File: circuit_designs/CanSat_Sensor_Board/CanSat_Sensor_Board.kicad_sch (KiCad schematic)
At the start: 19 parts

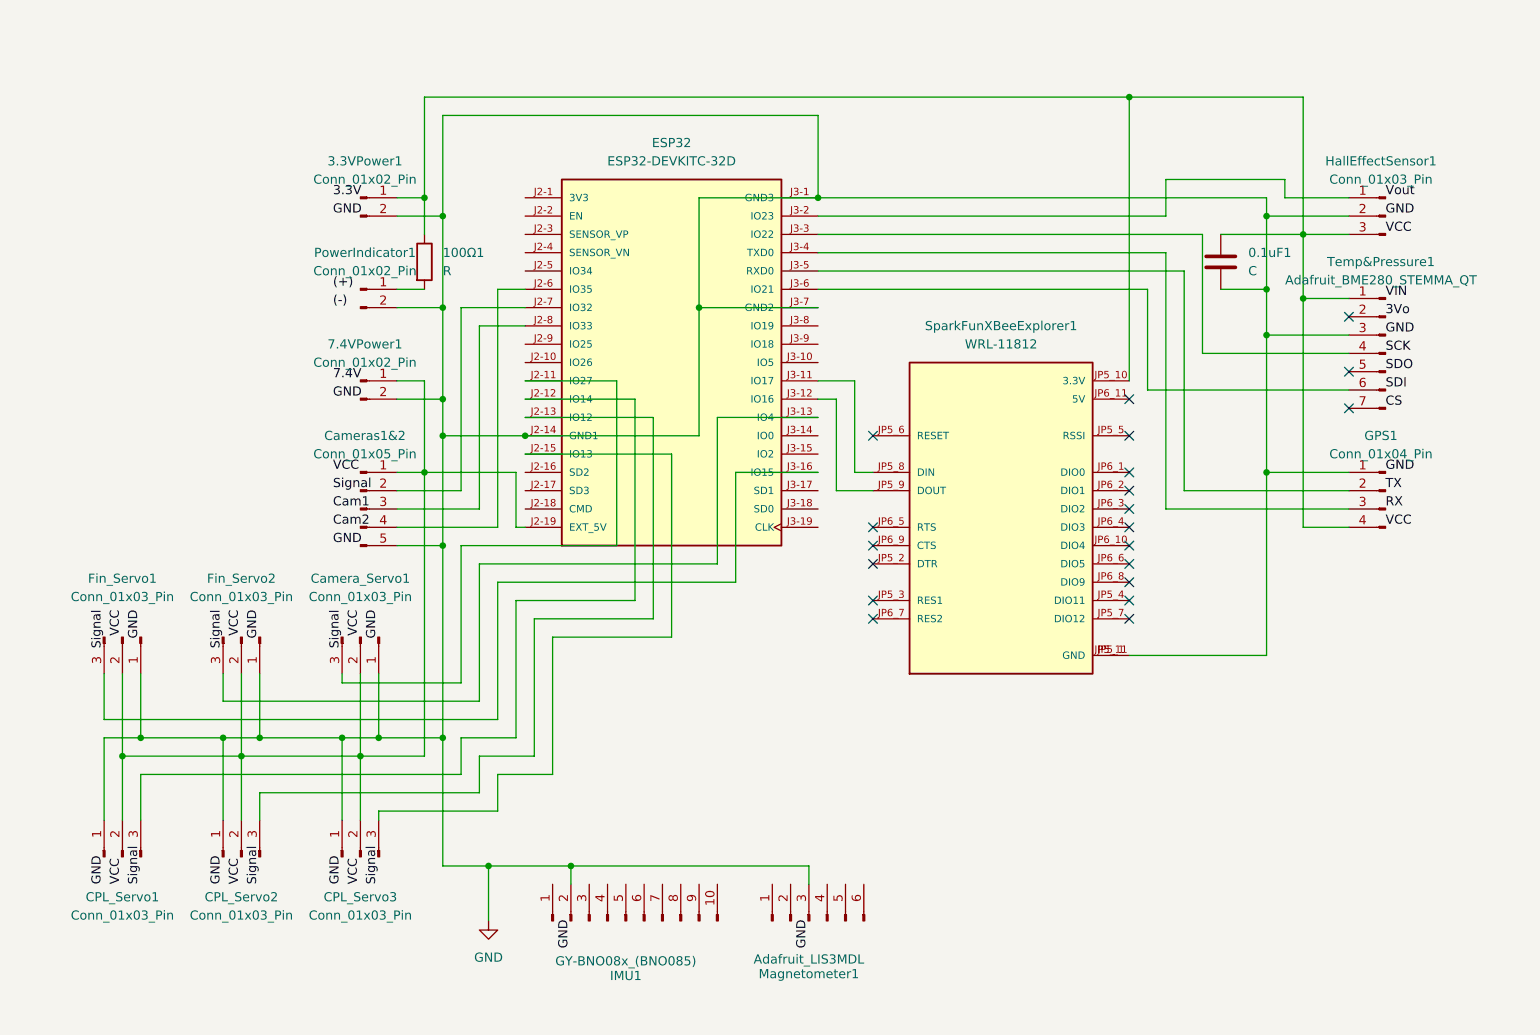
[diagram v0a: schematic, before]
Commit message: Adding all files including the schematics, layouts, and gerbers for the CanSat sensor and camera boards.
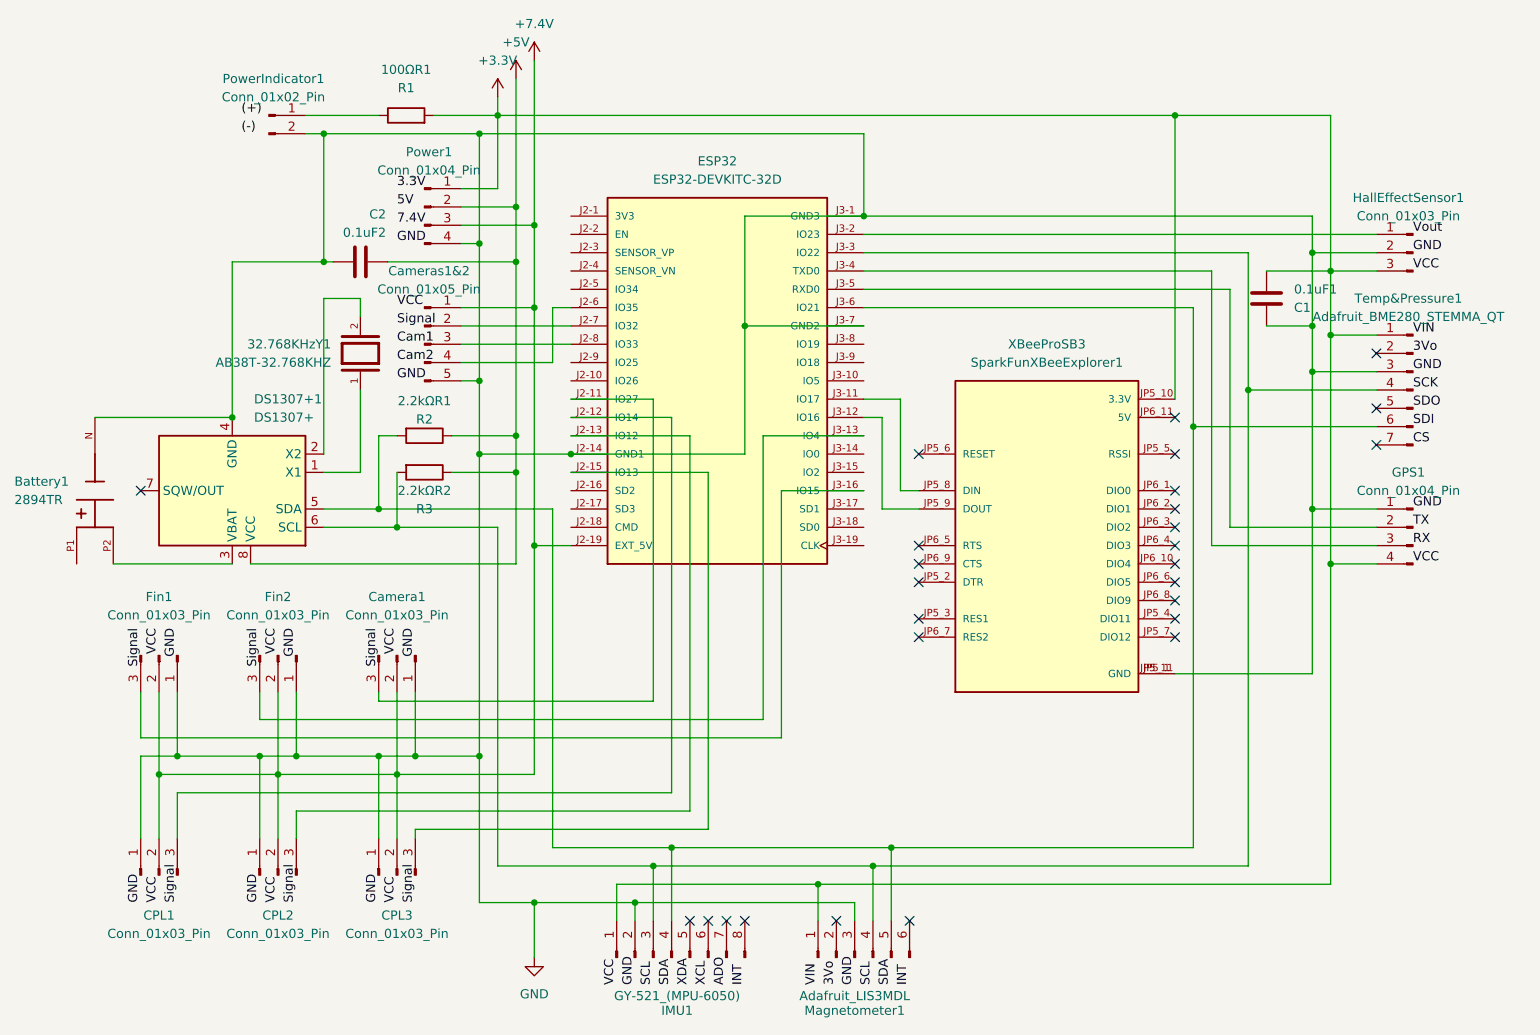
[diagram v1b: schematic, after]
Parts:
- removed 3.3VPower1, 7.4VPower1: Conn_01x02_Pin, Connector_JST:JST_PH_B2B-PH-K_1x02_P2.00mm_Vertical, symbol Connector:Conn_01x02_Pin
- removed IMU1: GY-BNO08x_(BNO085), Custom_Footprints:GY-BNO08x_(BNO085), symbol Connector:Conn_01x10_Pin
- added 0.1uF2: C2, Capacitor_SMD:C_0805_2012Metric_Pad1.18x1.45mm_HandSolder, symbol Device:C
- added 2.2kΩR1: R2, Resistor_THT:R_Axial_DIN0207_L6.3mm_D2.5mm_P7.62mm_Horizontal, symbol Device:R
- added 2.2kΩR2: R3, Resistor_THT:R_Axial_DIN0207_L6.3mm_D2.5mm_P7.62mm_Horizontal, symbol Device:R
- added 32.768KHzY1: AB38T-32.768KHZ, DigiKey:XTAL_AB38T-32.768KHZ, symbol AB38T-32.768KHZ:AB38T-32.768KHZ
- added Battery1: 2894TR, DigiKey:BAT_2894TR, symbol 2894TR:2894TR
- added DS1307+1: DS1307+, Package_DIP:DIP-8_W7.62mm, symbol Timer_RTC:DS1307+
- added IMU1: GY-521_(MPU-6050), Custom_Footprints:GY-521_(MPU-6050), symbol Connector:Conn_01x08_Pin
- added Power1: Conn_01x04_Pin, Connector_JST:JST_PH_B4B-PH-K_1x04_P2.00mm_Vertical, symbol Connector:Conn_01x04_Pin
- 0.1uF1: value C -> C1; footprint Capacitor_SMD:C_0201_0603Metric_Pad0.64x0.40mm_HandSolder -> Capacitor_SMD:C_0805_2012Metric_Pad1.18x1.45mm_HandSolder
- 100ΩR1: renamed from 100Ω1; value R -> R1
- ESP32: footprint ESP32-DEVKITC-32D:MODULE_ESP32-DEVKITC-32D -> Custom_Footprints:ESP32-WROOM-32D_Dev_Board
- XBeeProSB3: renamed from SparkFunXBeeExplorer1; value WRL-11812 -> SparkFunXBeeExplorer1
- renumbered CPL_Servo1 to CPL1, CPL_Servo2 to CPL2, CPL_Servo3 to CPL3, Camera_Servo1 to Camera1, Fin_Servo1 to Fin1, Fin_Servo2 to Fin2
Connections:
- net GND: now also 0.1uF2.1, Battery1.N, DS1307+1.4 (GND), IMU1.2 (Pin_2), Power1.4 (Pin_4)
- net +7.4V: now reaches CPL1.2 (Pin_2), CPL2.2 (Pin_2), CPL3.2 (Pin_2), Camera1.2 (Pin_2), Cameras1&2.1 (Pin_1), ESP32.J2-19 (EXT_5V), Fin1.2 (Pin_2), Fin2.2 (Pin_2)
- net +7.4V: now also Power1.3 (Pin_3)
- net +3.3V: now reaches 0.1uF1.1, GPS1.4 (Pin_4), HallEffectSensor1.3 (Pin_3), Temp&Pressure1.1 (Pin_1), XBeeProSB3.JP5_10 (3.3V)
- net +3.3V: now also 100ΩR1.2, Magnetometer1.1 (Pin_1), IMU1.1 (Pin_1), Power1.1 (Pin_1); no longer 100ΩR1.1
- net at PowerIndicator1.1 (Pin_1): now also 100ΩR1.1; no longer 100ΩR1.2
- net at Magnetometer1.4 (Pin_4): now also ESP32.J3-3 (IO22), Temp&Pressure1.4 (Pin_4), 2.2kΩR2.2, DS1307+1.6 (SCL), IMU1.3 (Pin_3)
- net at Magnetometer1.5 (Pin_5): now also ESP32.J3-6 (IO21), Temp&Pressure1.6 (Pin_6), 2.2kΩR1.2, DS1307+1.5 (SDA), IMU1.4 (Pin_4)
- new net: Battery1.P2, DS1307+1.3 (VBAT)
- new net: 32.768KHzY1.1, DS1307+1.1 (X1)
- new net: 32.768KHzY1.2, DS1307+1.2 (X2)
- new net +5V: 0.1uF2.2, 2.2kΩR1.1, 2.2kΩR2.1, DS1307+1.8 (VCC), Power1.2 (Pin_2)
- no-connect marks 20 -> 27
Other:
- moved on the sheet: 0.1uF1, 100ΩR1, CPL1, CPL2, CPL3, Camera1, Cameras1&2, ESP32, Fin1, Fin2, GPS1, HallEffectSensor1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
